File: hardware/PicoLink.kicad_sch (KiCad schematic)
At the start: 54 parts, among them J1 USB_C_Receptacle_GCT_USB4110-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, J2 USB_C_Receptacle_USB2.0_14P, J3 Conn_ARM_JTAG_SWD_10, J5 Conn_01x03, J6 Conn_01x03, SW1 434123025826_BTN, SW2 SW_Push, U1 W25Q16JV, U2 RP2040, U3 SWD_JTAG_10pin, U4 W25Q32JVSS, U5 AP2112K-3.3, U6 AMS1117-3.3, Y1 CSTNE12M0GH5L000R0

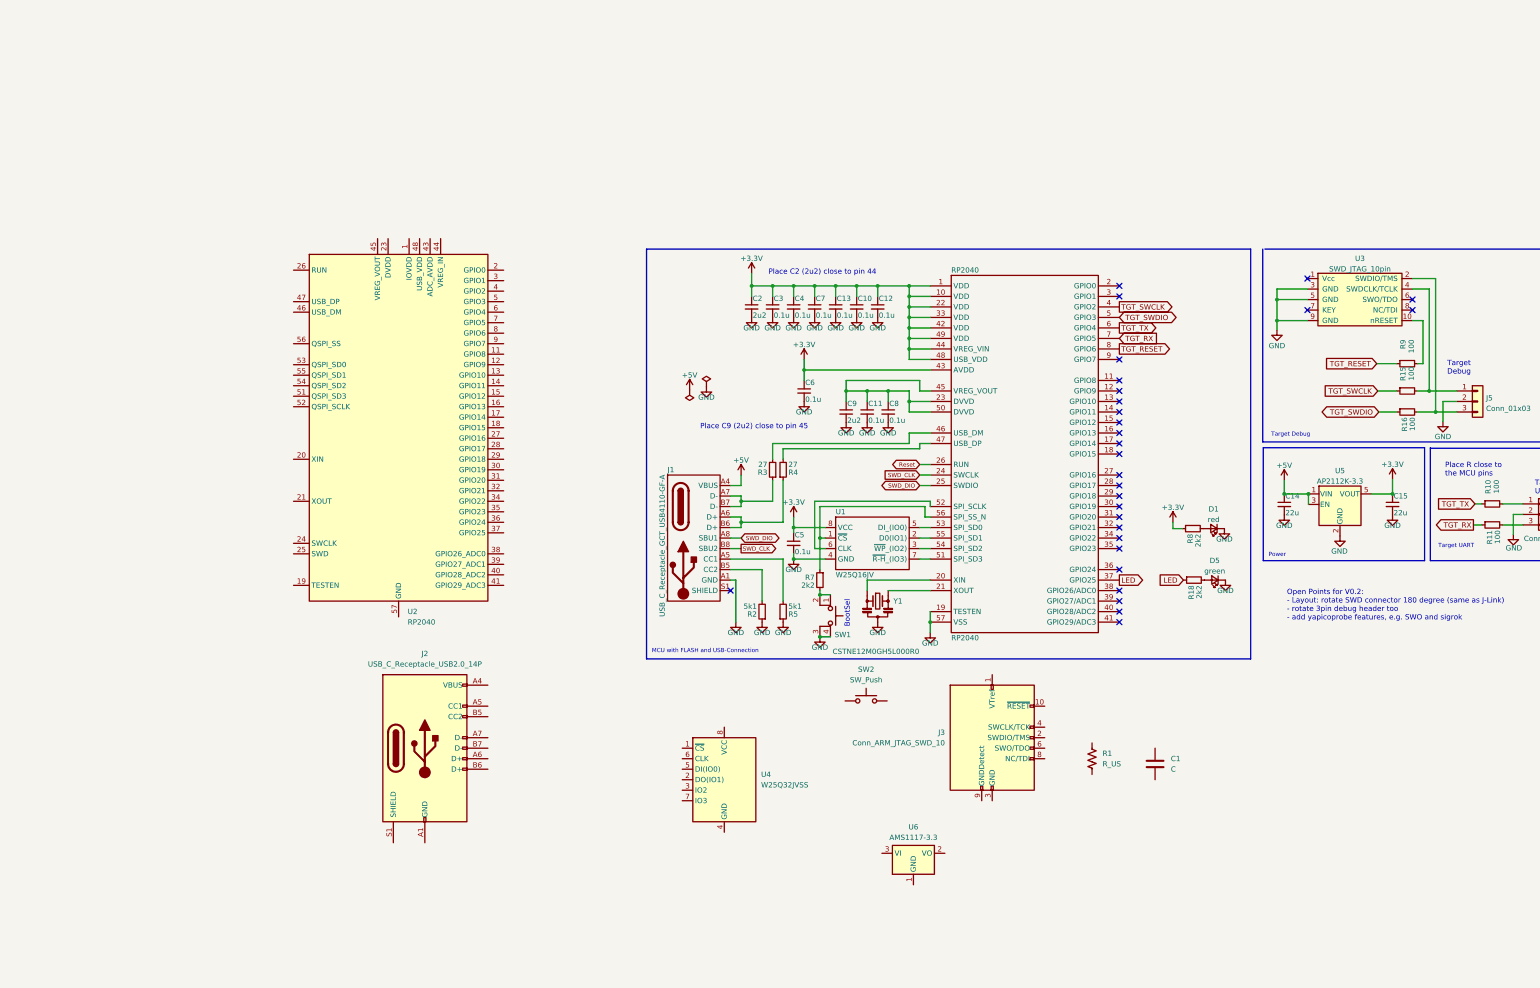
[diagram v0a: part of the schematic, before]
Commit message: [07-16-1503] small update on schematic
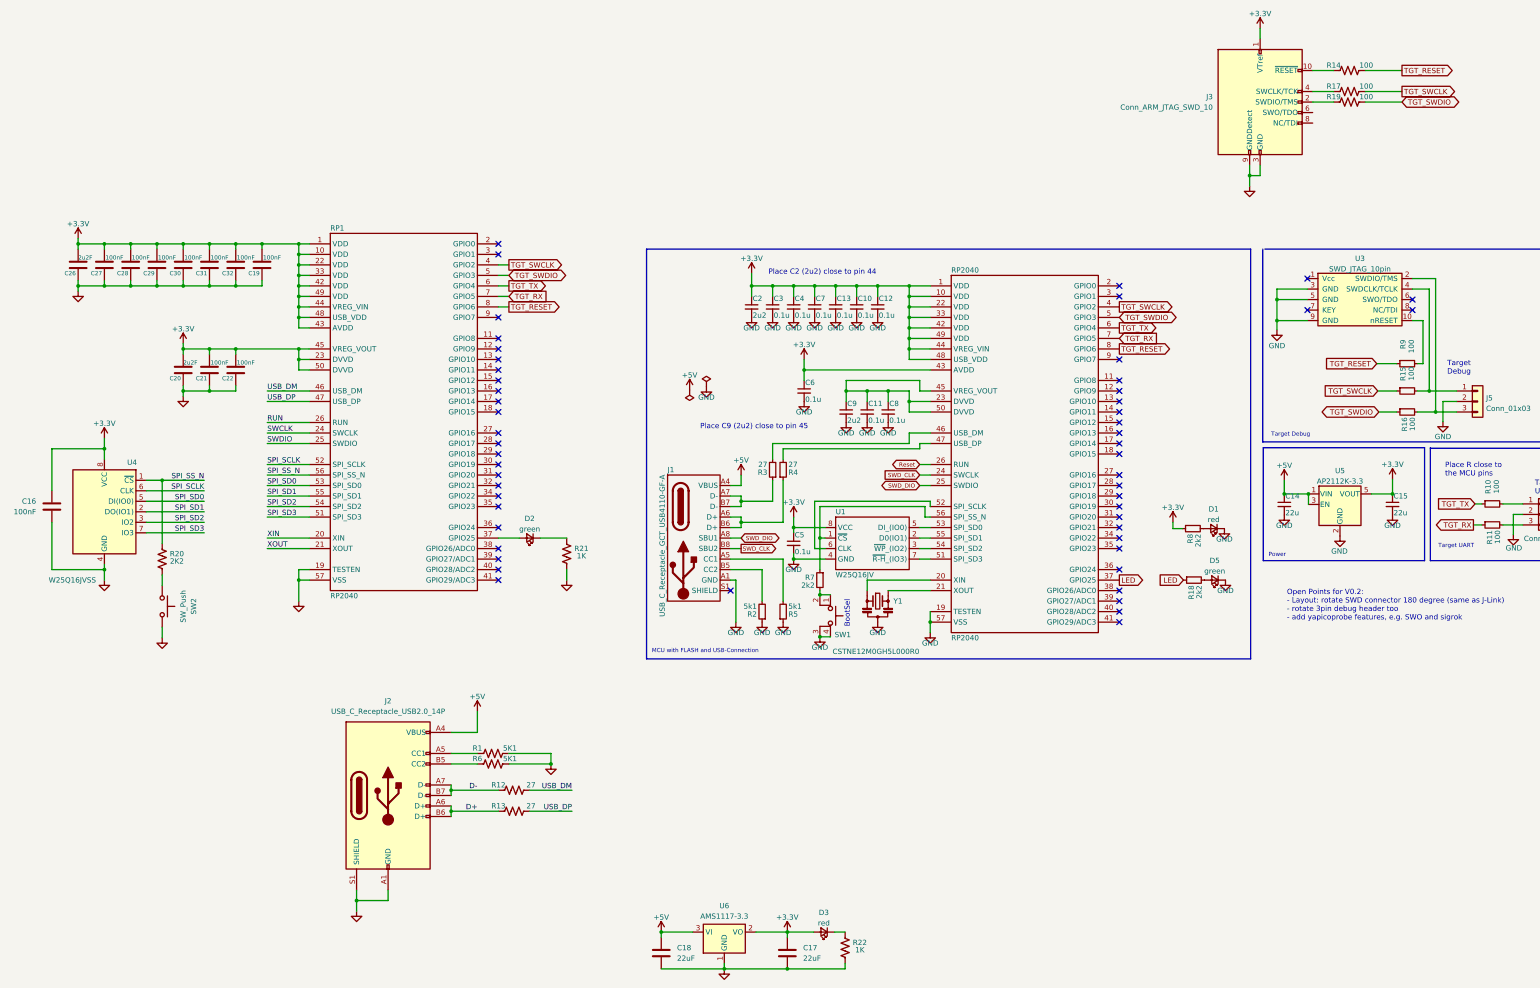
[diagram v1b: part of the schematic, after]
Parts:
- removed C1: C, symbol Device:C
- removed U2: RP2040, Package_DFN_QFN:QFN-56-1EP_7x7mm_P0.4mm_EP5.6x5.6mm, symbol MCU_RaspberryPi:RP2040
- added C16, C19, C21, C22, C27, C28, C29, C30, C31, C32: 100nF, symbol Device:C
- added C17, C18: 22uF, symbol Device:C
- added C20, C26: 2u2F, symbol Device:C
- added D2: green, McuOnEclipse:LED_0603, symbol Device:LED_Small
- added D3: red, McuOnEclipse:LED_0603, symbol Device:LED_Small
- added R12, R13: 27, symbol Device:R_US
- added R14, R17, R19: 100, symbol Device:R_US
- added R20: 2K2, symbol Device:R_US
- added R21, R22: 1K, symbol Device:R_US
- added R6: 5K1, symbol Device:R_US
- added RP1: RP2040, McuOnEclipse:QFN-56-1EP_7x7mm_P0.4mm_EP3.2x3.2mm, symbol McuOnEclipse:RP2040
- R1: value R_US -> 5K1
- U4: value W25Q32JVSS -> W25Q16JVSS
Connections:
- net +3.3V: now also J3.1 (VTref), U4.8 (VCC), U6.2 (VO), C16.1, C17.1, C19.1, C20.1, C21.1, C22.1, C26.1, C27.1, C28.1, C29.1, C30.1, C31.1, C32.1, D3.2 (A), RP1.1 (VDD), RP1.10 (VDD), RP1.22 (VDD), RP1.23 (DVVD), RP1.33 (VDD), RP1.42 (VDD), RP1.43 (AVDD), RP1.44 (VREG_VIN), RP1.45 (VREG_VOUT), RP1.48 (USB_VDD), RP1.49 (VDD), RP1.50 (DVVD)
- net +5V: now also J2.A4 (VBUS), J2.A9 (VBUS), J2.B4 (VBUS), J2.B9 (VBUS), U6.3 (VI), C18.1
- net GND: now also J2.A1 (GND), J2.A12 (GND), J2.B1 (GND), J2.B12 (GND), J2.S1 (SHIELD), J3.3 (GND), J3.5 (GND), J3.9 (GNDDetect), R1.2, SW2.2, U4.4 (GND), U6.1 (GND), C16.2, C17.2, C18.2, C19.2, C20.2, C21.2, C22.2, C26.2, C27.2, C28.2, C29.2, C30.2, C31.2, C32.2, R21.2, R22.2, R6.2, RP1.19 (TESTEN), RP1.57 (VSS)
- net TGT_RESET: now also R14.2, RP1.8 (GPIO6)
- net TGT_RX: now also RP1.7 (GPIO5)
- net TGT_SWCLK: now also R17.2, RP1.4 (GPIO2)
- net TGT_SWDIO: now also R19.2, RP1.5 (GPIO3)
- net TGT_TX: now also RP1.6 (GPIO4)
- net at J2.A5 (CC1): now also R1.1
- net D+: now reaches J2.A6 (D+)
- net D+: now also J2.B6 (D+), R13.1
- net D-: now reaches J2.A7 (D-)
- net D-: now also J2.B7 (D-), R12.1
- net at J2.B5 (CC2): now also R6.1
- net at J3.10 (~{RESET}): now also R14.1
- net at J3.2 (SWDIO/TMS): now also R19.1
- net at J3.4 (SWCLK/TCK): now also R17.1
- net at SW2.1: now also R20.2
- net SPI_SS_N: now reaches U4.1 (~{CS})
- net SPI_SS_N: now also R20.1, RP1.56 (SPI_SS_N)
- net SPI_SD1: now reaches U4.2 (DO(IO1))
- net SPI_SD1: now also RP1.55 (SPI_SD1)
- net SPI_SD2: now reaches U4.3 (IO2)
- net SPI_SD2: now also RP1.54 (SPI_SD2)
- net SPI_SD0: now reaches U4.5 (DI(IO0))
- net SPI_SD0: now also RP1.53 (SPI_SD0)
- net SPI_SCLK: now reaches U4.6 (CLK)
- net SPI_SCLK: now also RP1.52 (SPI_SCLK)
- net SPI_SD3: now reaches U4.7 (IO3)
- net SPI_SD3: now also RP1.51 (SPI_SD3)
- new net: D3.1 (K), R22.1
- new net: D2.1 (K), R21.1
- new net: D2.2 (A), RP1.37 (GPIO25)
- new net RUN: RP1.26 (RUN)
- new net SWCLK: RP1.24 (SWCLK)
- new net SWDIO: RP1.25 (SWDIO)
- new net USB_DM: R12.2, RP1.46 (USB_DM)
- new net USB_DP: R13.2, RP1.47 (USB_DP)
- new net XIN: RP1.20 (XIN)
- new net XOUT: RP1.21 (XOUT)
- no-connect marks 29 -> 53
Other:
- moved on the sheet: J2, J3, U4, U6

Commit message: [07-16-2030] finish rough routing
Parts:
- removed C10, C11, C12, C13, C3, C4, C5, C6, C7, C8: 0.1u, Capacitor_SMD:C_0603_1608Metric, symbol Device:C_Small
- removed C14, C15: 22u, McuOnEclipse:C_0805, symbol Device:C_Small
- removed C2, C9: 2u2, Capacitor_SMD:C_0603_1608Metric, symbol Device:C_Small
- removed D1: red, McuOnEclipse:LED_0603, symbol Device:LED_Small
- removed D5: green, McuOnEclipse:LED_0603, symbol Device:LED_Small
- removed H1: Logo HSLU, McuOnEclipse:Hochschule_Luzern_New, symbol Mechanical:MountingHole
- removed H2: QR, McuOnEclipse:QR_McuOnEclipse_Silkscreen, symbol Mechanical:MountingHole
- removed J1: USB_C_Receptacle_GCT_USB4110-GF-A, McuOnEclipse:USB_C_Receptacle_GCT_USB4110-GF-A, symbol McuOnEclipse:USB_C_Receptacle_GCT_USB4110-GF-A
- removed J5, J6: Conn_01x03, Connector_PinHeader_2.54mm:PinHeader_1x03_P2.54mm_Vertical, symbol Connector_Generic:Conn_01x03
- removed R10, R11, R15, R16, R9: 100, Resistor_SMD:R_0603_1608Metric, symbol Device:R_Small
- removed R18, R7, R8: 2k2, Resistor_SMD:R_0603_1608Metric, symbol Device:R_Small
- removed R2, R5: 5k1, Resistor_SMD:R_0603_1608Metric, symbol Device:R_Small
- removed R3, R4: 27, Resistor_SMD:R_0603_1608Metric, symbol Device:R_Small
- removed RP2040: RP2040, McuOnEclipse:QFN-56-1EP_7x7mm_P0.4mm_EP3.2x3.2mm, symbol McuOnEclipse:RP2040
- removed SW1: 434123025826_BTN, McuOnEclipse:434123025826_BTN, symbol Switch:SW_MEC_5E
- removed U1: W25Q16JV, McuOnEclipse:USON_2x3x0.6mm, symbol McuOnEclipse:W25Q16JV
- removed U3: SWD_JTAG_10pin, McuOnEclipse:SWD_Pin_Header_Straight_2x05_Pitch1.27mm_SMD, symbol McuOnEclipse:SWD_JTAG_10pin
- removed U5: AP2112K-3.3, McuOnEclipse:IC-SOT25, symbol Regulator_Linear:AP2112K-3.3
- removed Y1: CSTNE12M0GH5L000R0, McuOnEclipse:Resonator_SMD_Murata_CSTxExxV-3Pin_3.0x1.1mm, symbol McuOnEclipse:CSTNE12M0GH5L000R0
- added C1, C23: 12pF, Capacitor_SMD:C_0603_1608Metric_Pad1.08x0.95mm_HandSolder, symbol Device:C
- added J4: TARGET, Connector_PinHeader_2.54mm:PinHeader_1x03_P2.54mm_Vertical, symbol Connector_Generic:Conn_01x03
- added J7: UART, Connector_PinHeader_2.54mm:PinHeader_1x03_P2.54mm_Vertical, symbol Connector_Generic:Conn_01x03
- added J8: SIGROK_INPUT, Connector_PinHeader_2.54mm:PinHeader_1x07_P2.54mm_Horizontal, symbol Connector_Generic:Conn_01x08
- added J9: SIGROK_ADC, Connector_PinHeader_2.54mm:PinHeader_1x03_P2.54mm_Vertical, symbol Connector_Generic:Conn_01x03
- added R23, R24, R25, R26: 100, Resistor_SMD:R_0805_2012Metric_Pad1.20x1.40mm_HandSolder, symbol Device:R_US
- added U2: 74LVCH2T45DC, Package_SO:VSSOP-8_2.3x2mm_P0.5mm, symbol Logic_LevelTranslator:74LVCH2T45DC
- added Y2: 12Mhz HC49-SD, Crystal:Crystal_SMD_HC49-SD_HandSoldering, symbol Device:Crystal
- C16, C17, C18, C19, C20, C21, C22, C26, C27, C28, C29, C30, C31, C32: footprint (none) -> Capacitor_SMD:C_0603_1608Metric_Pad1.08x0.95mm_HandSolder
- D2, D3: footprint McuOnEclipse:LED_0603 -> LED_SMD:LED_0805_2012Metric_Pad1.15x1.40mm_HandSolder
- J2: footprint (none) -> Connector_USB:USB_C_Receptacle_GCT_USB4110
- J3: value Conn_ARM_JTAG_SWD_10 -> ARM_JTAG_10Pin; footprint Connector_PinHeader_1.27mm:PinHeader_2x05_P1.27mm_Vertical_SMD -> Connector_IDC:IDC-Header_2x05_P2.54mm_Vertical
- R1, R12, R13, R14, R17, R19, R20, R21, R22, R6: footprint (none) -> Resistor_SMD:R_0805_2012Metric_Pad1.20x1.40mm_HandSolder
- RP1: footprint McuOnEclipse:QFN-56-1EP_7x7mm_P0.4mm_EP3.2x3.2mm -> Package_DFN_QFN:QFN-56-1EP_7x7mm_P0.4mm_EP3.2x3.2mm
- SW2: value SW_Push -> BOOT SELECTOR; footprint (none) -> Button_Switch_SMD:SW_Push_1P1T_NO_6x6mm_H9.5mm
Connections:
- net RUN is gone; now on net Reset: RP1.26 (RUN)
- net SWCLK is gone; now on net SWD_CLK: RP1.24 (SWCLK)
- net SWDIO is gone; now on net SWD_DIO: RP1.25 (SWDIO)
- net GND: now also C1.2, C23.2, J4.2 (Pin_2), J7.2 (Pin_2)
- net TGT_RX: now also R26.1
- net TGT_SWCLK: now also R23.1
- net TGT_SWDIO: now also R24.1
- net TGT_TX: now also R25.1
- net XIN: now also C1.1, Y2.1
- net XOUT: now also C23.1, Y2.2
- net SIGROK_IN1: now reaches RP1.13 (GPIO10)
- net SIGROK_IN1: now also J8.1 (Pin_1)
- net SIGROK_IN2: now reaches RP1.14 (GPIO11)
- net SIGROK_IN2: now also J8.2 (Pin_2)
- net SIGROK_IN3: now reaches RP1.15 (GPIO12)
- net SIGROK_IN3: now also J8.3 (Pin_3)
- net SIGROK_IN4: now reaches RP1.16 (GPIO13)
- net SIGROK_IN4: now also J8.4 (Pin_4)
- net SIGROK_IN5: now reaches RP1.17 (GPIO14)
- net SIGROK_IN5: now also J8.5 (Pin_5)
- net SIGROK_IN6: now reaches RP1.18 (GPIO15)
- net SIGROK_IN6: now also J8.6 (Pin_6)
- net SIGROK_IN7: now reaches RP1.27 (GPIO16)
- net SIGROK_IN7: now also J8.7 (Pin_7)
- net SIGROK_IN8: now reaches RP1.28 (GPIO17)
- net SIGROK_IN8: now also J8.8 (Pin_8)
- net SWDIR: now reaches RP1.3 (GPIO1)
- net SIGROK_ADC0: now reaches RP1.38 (GPIO26/ADC0)
- net SIGROK_ADC0: now also J9.1 (Pin_1)
- net SIGROK_ADC1: now reaches RP1.39 (GPIO27/ADC1)
- net SIGROK_ADC1: now also J9.2 (Pin_2)
- net SIGROK_ADC2: now reaches RP1.40 (GPIO28/ADC2)
- net SIGROK_ADC2: now also J9.3 (Pin_3)
- new net: J4.1 (Pin_1), R23.2
- new net: J4.3 (Pin_3), R24.2
- new net: J7.3 (Pin_3), R26.2
- new net: J7.1 (Pin_1), R25.2
- no-connect marks 53 -> 14
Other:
- note added: "TODO: - Add Sigrok - Add Bidirectional Level Shifter"
- note removed: "BootSel"
- note removed: "MCU with FLASH and USB-Connection"
- note removed: "Open Points for V0.2: - Layout: rotate SWD connector 180 degree (same as J-Link) - rotate 3pin debug header too - add yapicoprobe features, e.g. SWO and sigrok"
- note removed: "Place C2 (2u2) close to pin 44"
- note removed: "Place C9 (2u2) close to pin 45"
- note removed: "Place R close to the MCU pins"
- note removed: "Power"
- note removed: "Target Debug"
- note removed: "Target UART"
- moved on the sheet: C16, C17, C18, C19, C20, C21, C22, C26, C27, C28, C29, C30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

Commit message: [07-17-1304] add edge cut
Update README.md
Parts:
- J8: footprint Connector_PinHeader_2.54mm:PinHeader_1x07_P2.54mm_Horizontal -> Connector_PinHeader_2.54mm:PinHeader_1x07_P2.54mm_Vertical
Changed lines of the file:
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@@
 	(label "SIGROK_IN8"
 		(at 204.47 71.12 180)
+		(fields_autoplaced yes)
 		(effects
 			(font
@@
 	(label "SIGROK_IN4"
 		(at 204.47 58.42 180)
+		(fields_autoplaced yes)
 		(effects
 			(font
@@
 	(label "SIGROK_IN7"
 		(at 204.47 68.58 180)
+		(fields_autoplaced yes)
 		(effects
 			(font
@@
 	(label "SIGROK_IN2"
 		(at 204.47 53.34 180)
+		(fields_autoplaced yes)
 		(effects
 			(font
@@
 	(label "SIGROK_IN3"
 		(at 204.47 55.88 180)
+		(fields_autoplaced yes)
 		(effects
 			(font
@@
 	(label "SIGROK_IN1"
 		(at 204.47 50.8 180)
+		(fields_autoplaced yes)
 		(effects
 			(font
@@
 	(label "SIGROK_IN5"
 		(at 204.47 60.96 180)
+		(fields_autoplaced yes)
 		(effects
 			(font
@@
 	(label "SIGROK_IN6"
 		(at 204.47 63.5 180)
+		(fields_autoplaced yes)
 		(effects
 			(font
@@
 			)
 		)
-		(property "Footprint" "Connector_PinHeader_2.54mm:PinHeader_1x07_P2.54mm_Horizontal"
+		(property "Footprint" "Connector_PinHeader_2.54mm:PinHeader_1x07_P2.54mm_Vertical"
 			(at 214.63 58.42 0)
 			(effects

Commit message: [07-17-1645] generate gerber files
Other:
- company: HSLU -> AHAH_TERROR
- title: PicoLink -> Piko
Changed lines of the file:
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@@
 	(paper "A4")
 	(title_block
-		(title "PicoLink")
-		(date "2023-02-27")
+		(title "Piko")
+		(date "2025-07-17")
 		(rev "V0.1")
-		(company "HSLU")
+		(company "AHAH_TERROR")
 	)
 	(junction

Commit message: [07-18-2108] add svg schematic
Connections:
- net +3.3V: no longer C20.1, C21.1, C22.1, RP1.23 (DVVD), RP1.45 (VREG_VOUT), RP1.50 (DVVD)
- new net: C20.1, C21.1, C22.1, RP1.23 (DVVD), RP1.45 (VREG_VOUT), RP1.50 (DVVD)
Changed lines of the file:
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@@
 	)
 	(junction
+		(at 127 48.26)
+		(diameter 0)
+		(color 0 0 0 0)
+	)
+	(junction
 		(at 88.9 33.02)
 		(diameter 0)
@@
 	)
 	(junction
+		(at 120.65 48.26)
+		(diameter 0)
+		(color 0 0 0 0)
+	)
+	(junction
 		(at 142.24 22.86)
 		(diameter 0)
@@
 	)
 	(junction
-		(at 127 48.26)
-		(diameter 0)
-		(color 0 0 0 0)
-	)
-	(junction
 		(at 120.65 33.02)
 		(diameter 0)
@@
 	)
 	(junction
-		(at 120.65 48.26)
-		(diameter 0)
-		(color 0 0 0 0)
-	)
-	(junction
 		(at 127 22.86)
 		(diameter 0)
@@
 	)
 	(junction
-		(at 114.3 48.26)
-		(diameter 0)
-		(color 0 0 0 0)
-	)
-	(junction
 		(at 142.24 27.94)
 		(diameter 0)
@@
 	(wire
 		(pts
-			(xy 142.24 40.64) (xy 142.24 43.18)
+			(xy 114.3 48.26) (xy 120.65 48.26)
 		)
 		(stroke
@@
 	(wire
 		(pts
-			(xy 142.24 22.86) (xy 144.78 22.86)
+			(xy 142.24 40.64) (xy 142.24 43.18)
 		)
 		(stroke
@@
 	(wire
 		(pts
-			(xy 193.04 30.48) (xy 190.5 30.48)
+			(xy 142.24 22.86) (xy 144.78 22.86)
 		)
 		(stroke
@@
 	(wire
 		(pts
-			(xy 127 22.86) (xy 127 24.13)
+			(xy 193.04 30.48) (xy 190.5 30.48)
 		)
 		(stroke
@@
 	(wire
 		(pts
-			(xy 127 48.26) (xy 127 49.53)
+			(xy 127 22.86) (xy 127 24.13)
 		)
 		(stroke
@@
 	(wire
 		(pts
+			(xy 127 48.26) (xy 127 49.53)
+		)
+		(stroke
+			(width 0)
+			(type default)
+		)
+	)
+	(wire
+		(pts
 			(xy 180.34 152.4) (xy 180.34 153.67)
 		)
@@
 	(wire
 		(pts
-			(xy 114.3 48.26) (xy 120.65 48.26)
+			(xy 134.62 66.04) (xy 144.78 66.04)
 		)
 		(stroke
@@
 	(wire
 		(pts
-			(xy 134.62 66.04) (xy 144.78 66.04)
+			(xy 120.65 48.26) (xy 120.65 49.53)
 		)
 		(stroke
@@
 	(wire
 		(pts
+			(xy 120.65 48.26) (xy 127 48.26)
+		)
+		(stroke
+			(width 0)
+			(type default)
+		)
+	)
+	(wire
+		(pts
 			(xy 40.64 129.54) (xy 35.56 129.54)
 		)
@@
 	(wire
 		(pts
-			(xy 120.65 48.26) (xy 127 48.26)
+			(xy 59.69 83.82) (xy 59.69 81.28)
 		)
 		(stroke
@@
 	(wire
 		(pts
-			(xy 59.69 83.82) (xy 59.69 81.28)
+			(xy 101.6 31.75) (xy 101.6 33.02)
 		)
 		(stroke
@@
 	(wire
 		(pts
-			(xy 101.6 31.75) (xy 101.6 33.02)
+			(xy 95.25 33.02) (xy 101.6 33.02)
 		)
 		(stroke
@@
 	(wire
 		(pts
-			(xy 95.25 33.02) (xy 101.6 33.02)
+			(xy 114.3 48.26) (xy 114.3 49.53)
 		)
 		(stroke
@@
 	(wire
 		(pts
-			(xy 120.65 48.26) (xy 120.65 49.53)
-		)
-		(stroke
-			(width 0)
-			(type default)
-		)
-	)
-	(wire
-		(pts
 			(xy 134.62 158.75) (xy 146.05 158.75)
 		)
@@
 	(wire
 		(pts
-			(xy 114.3 46.99) (xy 114.3 48.26)
-		)
-		(stroke
-			(width 0)
-			(type default)
-		)
-	)
-	(wire
-		(pts
 			(xy 69.85 58.42) (xy 55.88 58.42)
 		)
@@
 	(wire
 		(pts
-			(xy 127 48.26) (xy 142.24 48.26)
-		)
-		(stroke
-			(width 0)
-			(type default)
-		)
-	)
-	(wire
-		(pts
 			(xy 95.25 22.86) (xy 101.6 22.86)
 		)
@@
 	(wire
 		(pts
+			(xy 127 48.26) (xy 142.24 48.26)
+		)
+		(stroke
+			(width 0)
+			(type default)
+		)
+	)
+	(wire
+		(pts
 			(xy 54.61 167.64) (xy 49.53 167.64)
 		)
@@
 	(wire
 		(pts
-			(xy 114.3 48.26) (xy 114.3 49.53)
-		)
-		(stroke
-			(width 0)
-			(type default)
-		)
-	)
-	(wire
-		(pts
 			(xy 132.08 97.79) (xy 129.54 97.79)
 		)
@@
 					(unit 1)
 				)
-			)
-		)
-	)
-	(symbol
-		(lib_id "power:+3.3V")
-		(at 114.3 46.99 0)
-		(unit 1)
-		(exclude_from_sim no)
-		(in_bom yes)
-		(on_board yes)
-		(dnp no)
-		(property "Reference" "#PWR020"
-			(at 114.3 50.8 0)
-			(effects
-				(font
-					(size 1.27 1.27)
-				)
-				(hide yes)
-			)
-		)
-		(property "Value" "+3.3V"
-			(at 114.3 43.4142 0)
-			(effects
-				(font
-					(size 1.27 1.27)
-				)
-			)
-		)
-		(property "Footprint" ""
-			(at 114.3 46.99 0)
-			(effects
-				(font
-					(size 1.27 1.27)
-				)
-				(hide yes)
-			)
-		)
-		(property "Datasheet" ""
-			(at 114.3 46.99 0)
-			(effects
-				(font
-					(size 1.27 1.27)
-				)
-				(hide yes)
-			)
-		)
-		(property "Description" ""
-			(at 114.3 46.99 0)
-			(effects
-				(font
-					(size 1.27 1.27)
-				)
-				(hide yes)
-			)
-		)
-		(pin "1"
-		)
-		(instances
-			(project "PicoLink"
-				(path "/acad0ee0-2ac2-4516-b2b7-53e1758dc208"
-					(reference "#PWR020")
-					(unit 1)
-				)
